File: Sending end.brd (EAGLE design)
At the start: 100 x 80 mm, 17 parts, among them IC1 MEGA8-P

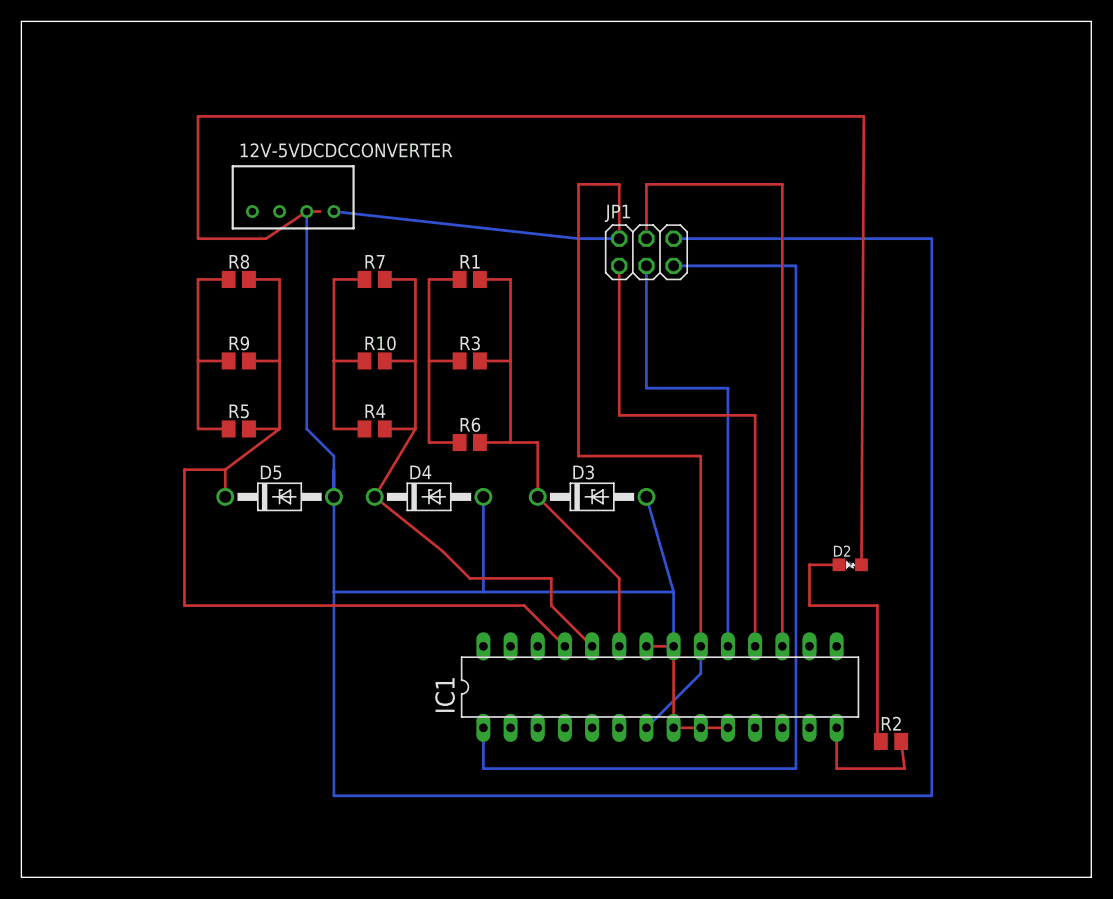
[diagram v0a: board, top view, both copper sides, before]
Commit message: The Sending End layout before going through the checklist
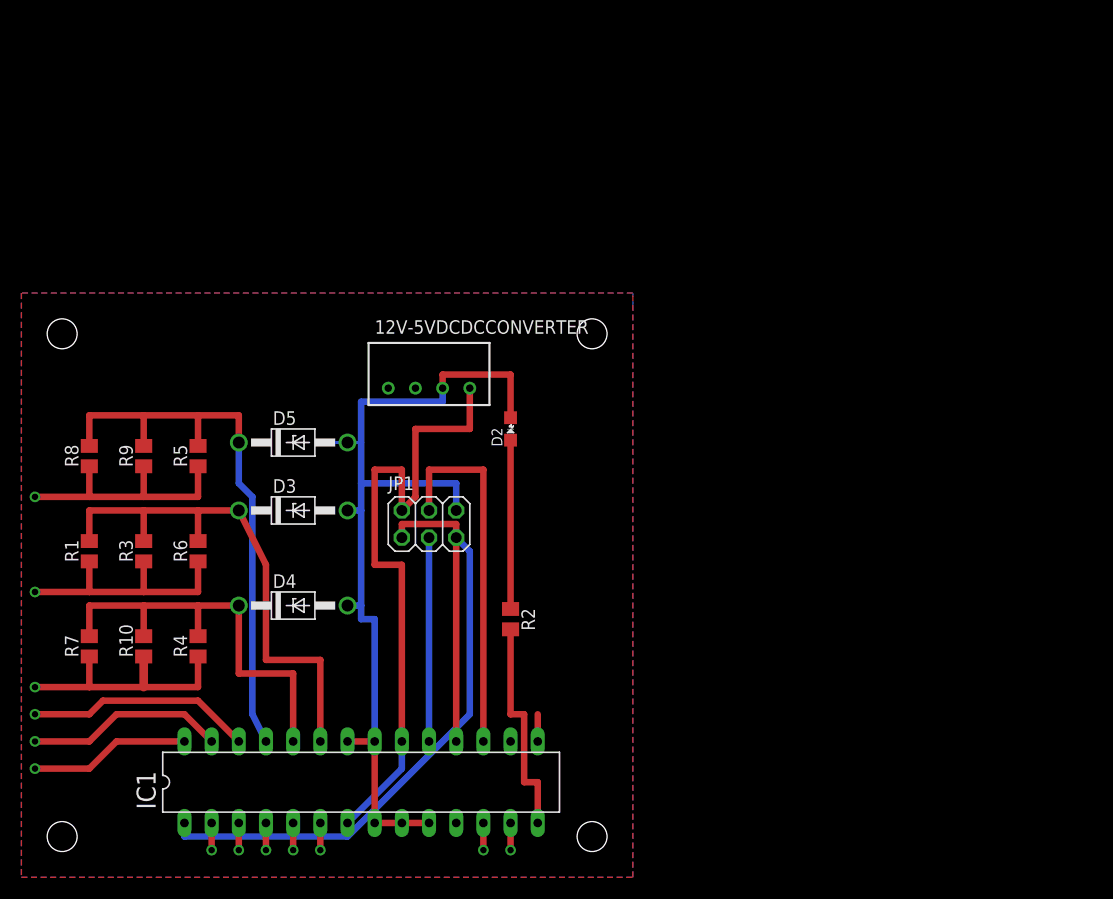
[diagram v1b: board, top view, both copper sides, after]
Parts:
- moved R1 43.7 mm to (6.35, 30.5), turned to 90 degrees
- moved R7 43.4 mm to (6.35, 21.6), turned to 90 degrees
- moved R2 37.4 mm to (45.7, 24.1), turned to 270 degrees
- moved R3 35.3 mm to (11.4, 30.5), turned to 90 degrees
- moved R10 34.3 mm to (11.4, 21.6), turned to 90 degrees
- moved D2 34.2 mm to (45.7, 41.9), turned to 90 degrees
- moved JP1 32.5 mm to (38.1, 33.0)
- moved IC1 29.3 mm to (31.8, 8.89)
- moved D3 28.0 mm to (25.4, 34.3)
- moved R6 27.4 mm to (16.5, 30.5), turned to 90 degrees
- moved R4 26.2 mm to (16.5, 21.6), turned to 90 degrees
- moved R8 21.6 mm to (6.35, 39.4), turned to 90 degrees
- moved 12V-5VDCDCCONVERTER 20.8 mm to (38.1, 45.7)
- moved D4 16.3 mm to (25.4, 25.4)
- moved R9 12.6 mm to (11.4, 39.4), turned to 90 degrees
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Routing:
- net GND: track 388.3 -> 86.6 mm
- net N$7: track 91.4 -> 49.7 mm
- net VCC: track 100.0 -> 61.1 mm
- net N$3: track 85.1 -> 53.9 mm
- net N$23: track 61.0 -> 34.3 mm
- net N$25: track 43.2 -> 19.1 mm
- net N$24: track 48.3 -> 26.7 mm
- net N$11: track 0.00 -> 21.2 mm, vias 0 -> 1
- net N$12: track 0.00 -> 18.6 mm, vias 0 -> 1
- net N$2: track 57.2 -> 40.3 mm
- net N$13: track 0.00 -> 15.0 mm, vias 0 -> 1
- net N$6: track 25.9 -> 15.8 mm
- net N$20: track 12.7 -> 20.6 mm
- net N$21: track 0.00 -> 2.54 mm
- net N$19: track 0.00 -> 2.54 mm, vias 0 -> 1
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- added copper zone on layer 16, net N$4
- added copper zone on layer 1, net N$9
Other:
- board outline removed
- board text added: "Night Rider: Transmission Board"
- board text added: "Solomon Cooper Jessie Bates Brandon Valentine Abdullah Al Madan"

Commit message: Sending End Layout before meeting with Greenberg
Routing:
- net N$7: track 49.7 -> 62.0 mm
- net N$21: track 2.54 -> 13.0 mm, vias 0 -> 1
- net N$24: track 26.7 -> 21.2 mm
- net VCC: track 61.1 -> 58.3 mm
- net GND: track 86.6 -> 84.3 mm
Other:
- board text added: "Version 2.0"
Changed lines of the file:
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@@
 <setting verticaltext="up"/>
 </settings>
-<grid distance="0.05" unitdist="inch" unit="inch" style="lines" multiple="1" display="no" altdistance="0.025" altunitdist="inch" altunit="inch"/>
+<grid distance="0.01" unitdist="inch" unit="inch" style="lines" multiple="1" display="yes" altdistance="0.025" altunitdist="inch" altunit="inch"/>
 <layers>
 <layer number="1" name="Top" color="4" fill="1" visible="yes" active="yes"/>
@@
 <hole x="53.34" y="3.81" drill="2.8"/>
 <hole x="53.34" y="50.8" drill="2.8"/>
-<text x="6.35" y="50.8" size="1.27" layer="48" distance="47">Night Rider: Transmission Board</text>
-<text x="6.35" y="44.45" size="1.016" layer="48">Solomon Cooper
+<text x="6.604" y="52.578" size="1.27" layer="21" distance="47">Night Rider: Transmission Board</text>
+<text x="6.096" y="44.958" size="1.27" layer="21">Solomon Cooper
 Jessie Bates
 Brandon Valentine
 Abdullah Al Madan</text>
+<text x="5.08" y="1.27" size="1.4224" layer="21">Version 2.0</text>
 </plain>
 <attributes>
@@
 <wire x1="33.02" y1="12.7" x2="33.02" y2="5.08" width="0.6096" layer="1"/>
 <wire x1="31.75" y1="36.83" x2="31.75" y2="40.64" width="0.6096" layer="16"/>
-<wire x1="27.94" y1="40.64" x2="30.48" y2="40.64" width="0.254" layer="16"/>
+<wire x1="30.226" y1="40.64" x2="30.48" y2="40.64" width="0.254" layer="16"/>
 <wire x1="30.48" y1="40.64" x2="31.75" y2="40.64" width="0.254" layer="16"/>
 <wire x1="31.75" y1="34.29" x2="31.75" y2="36.83" width="0.6096" layer="16"/>
@@
 <wire x1="7.62" y1="16.51" x2="6.35" y2="15.24" width="0.6096" layer="1"/>
 <wire x1="6.35" y1="15.24" x2="1.27" y2="15.24" width="0.6096" layer="1"/>
-<via x="1.27" y="15.24" extent="1-16" drill="0.6" shape="square"/>
+<via x="1.27" y="15.24" extent="1-16" drill="0.5"/>
 </signal>
 <signal name="N$12">
@@
 <wire x1="8.89" y1="15.24" x2="6.35" y2="12.7" width="0.6096" layer="1"/>
 <wire x1="6.35" y1="12.7" x2="1.27" y2="12.7" width="0.6096" layer="1"/>
-<via x="1.27" y="12.7" extent="1-16" drill="0.6" shape="square"/>
+<via x="1.27" y="12.7" extent="1-16" drill="0.5"/>
 </signal>
 <signal name="N$13">
@@
 <wire x1="8.89" y1="12.7" x2="6.35" y2="10.16" width="0.6096" layer="1"/>
 <wire x1="6.35" y1="10.16" x2="1.27" y2="10.16" width="0.6096" layer="1"/>
-<via x="1.27" y="10.16" extent="1-16" drill="0.6" shape="square"/>
+<via x="1.27" y="10.16" extent="1-16" drill="0.5"/>
 </signal>
 <signal name="N$14">
 <contactref element="IC1" pad="2"/>
 <wire x1="17.78" y1="5.08" x2="17.78" y2="2.54" width="0.6096" layer="1"/>
-<via x="17.78" y="2.54" extent="1-16" drill="0.6" shape="square"/>
+<via x="17.78" y="2.54" extent="1-16" drill="0.5"/>
 </signal>
 <signal name="N$15">
 <contactref element="IC1" pad="3"/>
 <wire x1="20.32" y1="5.08" x2="20.32" y2="2.54" width="0.6096" layer="1"/>
-<via x="20.32" y="2.54" extent="1-16" drill="0.6" shape="square"/>
+<via x="20.32" y="2.54" extent="1-16" drill="0.5"/>
 </signal>
 <signal name="N$16">
 <contactref element="IC1" pad="4"/>
 <wire x1="22.86" y1="5.08" x2="22.86" y2="2.54" width="0.6096" layer="1"/>
-<via x="22.86" y="2.54" extent="1-16" drill="0.6" shape="square"/>
+<via x="22.86" y="2.54" extent="1-16" drill="0.5"/>
 </signal>
 <signal name="N$17">
 <contactref element="IC1" pad="6"/>
 <wire x1="27.94" y1="5.08" x2="27.94" y2="2.54" width="0.6096" layer="1"/>
-<via x="27.94" y="2.54" extent="1-16" drill="0.6" shape="square"/>
+<via x="27.94" y="2.54" extent="1-16" drill="0.5"/>
 </signal>
 <signal name="N$18">
 <contactref element="IC1" pad="12"/>
 <wire x1="43.18" y1="5.08" x2="43.18" y2="2.54" width="0.6096" layer="1"/>
-<via x="43.18" y="2.54" extent="1-16" drill="0.6" shape="square"/>
+<via x="43.18" y="2.54" extent="1-16" drill="0.5"/>
 </signal>
 <signal name="N$19">
 <contactref element="IC1" pad="13"/>
 <wire x1="45.72" y1="5.08" x2="45.72" y2="2.54" width="0.6096" layer="1"/>
-<via x="45.72" y="2.54" extent="1-16" drill="0.6" shape="square"/>
+<via x="45.72" y="2.54" extent="1-16" drill="0.5"/>
 </signal>
 <signal name="N$20">
@@
 <signal name="N$21">
 <contactref element="IC1" pad="15"/>
-<wire x1="48.26" y1="12.7" x2="48.26" y2="15.24" width="0.6096" layer="1"/>
+<wire x1="48.26" y1="12.7" x2="51.054" y2="12.7" width="0.6096" layer="1"/>
+<wire x1="51.054" y1="12.7" x2="51.054" y2="2.54" width="0.6096" layer="1"/>
+<via x="51.054" y="2.54" extent="1-16" drill="0.5"/>
 </signal>
 <signal name="N$22">
@@
 <contactref element="IC1" pad="18"/>
 <contactref element="JP1" pad="1"/>
-<wire x1="35.56" y1="31.75" x2="35.56" y2="33.02" width="0.6096" layer="1"/>
-<wire x1="35.56" y1="33.02" x2="40.64" y2="33.02" width="0.6096" layer="1"/>
-<wire x1="40.64" y1="33.02" x2="40.64" y2="12.7" width="0.6096" layer="1"/>
+<wire x1="35.56" y1="31.75" x2="35.56" y2="30.226" width="0.6096" layer="1"/>
+<wire x1="35.56" y1="30.226" x2="40.64" y2="25.4" width="0.6096" layer="1"/>
+<wire x1="40.64" y1="25.4" x2="40.64" y2="12.7" width="0.6096" layer="1"/>
 </signal>
 <signal name="N$25">
@@
 <contactref element="IC1" pad="1"/>
 <contactref element="JP1" pad="5"/>
-<wire x1="15.24" y1="3.81" x2="15.24" y2="5.08" width="0.6096" layer="16"/>
-<wire x1="30.48" y1="3.81" x2="15.24" y2="3.81" width="0.6096" layer="16"/>
+<wire x1="15.24" y1="1.016" x2="15.24" y2="5.08" width="0.6096" layer="16"/>
+<wire x1="30.988" y1="1.016" x2="15.24" y2="1.016" width="0.6096" layer="16"/>
 <wire x1="40.64" y1="31.75" x2="41.91" y2="30.48" width="0.6096" layer="16"/>
 <wire x1="41.91" y1="30.48" x2="41.91" y2="15.24" width="0.6096" layer="16"/>
-<wire x1="41.91" y1="15.24" x2="30.48" y2="3.81" width="0.6096" layer="16"/>
+<wire x1="41.91" y1="15.24" x2="41.91" y2="1.016" width="0.6096" layer="16"/>
+<wire x1="41.91" y1="1.016" x2="30.988" y2="1.016" width="0.6096" layer="16"/>
 </signal>
 <signal name="VCC">
@@
 <wire x1="35.56" y1="10.16" x2="30.48" y2="5.08" width="0.6096" layer="16"/>
 <wire x1="35.56" y1="12.7" x2="35.56" y2="10.16" width="0.6096" layer="16"/>
-<wire x1="35.56" y1="34.29" x2="36.83" y2="35.56" width="0.6096" layer="1"/>
-<wire x1="36.83" y1="35.56" x2="36.83" y2="41.91" width="0.6096" layer="1"/>
-<wire x1="36.83" y1="41.91" x2="41.91" y2="41.91" width="0.6096" layer="1"/>
+<wire x1="35.56" y1="34.29" x2="35.56" y2="38.354" width="0.6096" layer="1"/>
+<wire x1="35.56" y1="38.354" x2="38.608" y2="41.91" width="0.6096" layer="1"/>
+<wire x1="38.608" y1="41.91" x2="41.91" y2="41.91" width="0.6096" layer="1"/>
 <wire x1="41.91" y1="41.91" x2="41.91" y2="45.72" width="0.6096" layer="1"/>
-<wire x1="35.56" y1="29.21" x2="35.56" y2="12.7" width="0.6096" layer="1"/>
-<wire x1="33.02" y1="29.21" x2="35.56" y2="29.21" width="0.6096" layer="1"/>
+<wire x1="35.56" y1="26.416" x2="35.56" y2="12.7" width="0.6096" layer="1"/>
+<wire x1="33.02" y1="29.21" x2="35.56" y2="26.416" width="0.6096" layer="1"/>
 <wire x1="35.56" y1="34.29" x2="35.56" y2="38.1" width="0.6096" layer="1"/>
 <wire x1="35.56" y1="38.1" x2="33.02" y2="38.1" width="0.6096" layer="1"/>
@@
 <contactref element="IC1" pad="5"/>
 <wire x1="25.4" y1="5.08" x2="25.4" y2="2.54" width="0.6096" layer="1"/>
-<via x="25.4" y="2.54" extent="1-16" drill="0.6" shape="square"/>
+<via x="25.4" y="2.54" extent="1-16" drill="0.5"/>
 </signal>
 <signal name="N$2">
@@
 <wire x1="11.43" y1="26.67" x2="11.43" y2="29.53" width="0.6096" layer="1"/>
 <wire x1="6.35" y1="26.67" x2="1.27" y2="26.67" width="0.6096" layer="1"/>
-<via x="1.27" y="26.67" extent="1-16" drill="0.6" shape="square"/>
+<via x="1.27" y="26.67" extent="1-16" drill="0.5"/>
 </signal>
 <signal name="N$8">
@@
 <wire x1="11.43" y1="17.78" x2="11.43" y2="20.64" width="0.8128" layer="1"/>
 <wire x1="6.35" y1="17.78" x2="1.27" y2="17.78" width="0.6096" layer="1"/>
-<via x="1.27" y="17.78" extent="1-16" drill="0.6" shape="square"/>
+<via x="1.27" y="17.78" extent="1-16" drill="0.5"/>
 </signal>
 <signal name="N$10">
@@
 <wire x1="11.43" y1="35.56" x2="11.43" y2="38.42" width="0.6096" layer="1"/>
 <wire x1="6.35" y1="35.56" x2="1.27" y2="35.56" width="0.6096" layer="1"/>
-<via x="1.27" y="35.56" extent="1-16" drill="0.6" shape="square"/>
+<via x="1.27" y="35.56" extent="1-16" drill="0.5"/>
 </signal>
 <signal name="N$4">

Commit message: sending end echematic version 3.0. need more work on the DCDC converter
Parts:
- removed D3, D4, D5: ZPY, diode:DO41Z10
- removed R1, R10, R3, R4, R5, R6, R7, R8, R9: tbd, resistor:M0805
- added C1, C2, C3, C4, C5, C6, C7: (no value), rcl:C0805
- added R12, R13, R14, R15, R16, R17, R18, R19, R20: tbd, resistor:M0805
- added R21: 10k, resistor:M0805
- added T1, T2, T3: (no value), zetex:SOT-23
- added TP1, TP10, TP11, TP12, TP13, TP14, TP2, TP3, TP4, TP5, TP6, TP7, TP8, TP9: PTR1PAD1-20, testpad:P1-20
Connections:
- removed net N$10: R5.1, R8.1, R9.1
- removed net N$2: D4.C, IC1.24, R10.2, R4.2, R7.2
- removed net N$26: D3.C, IC1.23, R1.2, R3.2, R6.2
- removed net N$3: D5.C, IC1.25, R5.2, R8.2, R9.2
- removed net N$5: R1.1, R3.1, R6.1
- removed net N$8: R10.1, R4.1, R7.1
- new net AVCC: IC1.20
- new net LEFT: R17.1
- new net N$12: IC1.9, TP1.TP
- new net N$31: C1.2, C6.2
- new net N$34: C4.1, R16.2, R17.2, T2.3
- new net N$35: R15.2, T2.1
- new net N$37: C5.1, R19.2, R20.2, T3.3
- new net N$39: IC1.10, TP3.TP
- new net N$40: IC1.11, TP8.TP
- new net N$41: IC1.26, R12.2, T1.1
- new net RIGHT: R14.1
- new net STOP: R20.1
- new net VCC1: C7.1
- net GND: now also C2.2, C3.2, C4.2, C5.2, C7.2, R13.1, R16.1, R19.1, T1.2, T2.2, T3.2; no longer D3.A, D4.A, D5.A, IC1.10, IC1.9
- net N$1: now also TP5.TP
- net N$11: now also C3.1, R13.2, R14.2, T1.3; no longer IC1.26
- net N$13: now also R18.2, T3.1
- net N$15: now also TP4.TP
- net N$16: now also TP7.TP
- net N$17: now also TP6.TP
- net N$18: now also TP9.TP
- net N$19: now also TP10.TP
- net N$21: now also TP13.TP
- net N$22: now also TP14.TP
- net N$27: now also TP11.TP
- net N$28: now also TP12.TP
- net N$7: now also R21.2
- net VCC: now also C1.1, C6.1, R12.1, R15.1, R18.1, R21.1; no longer IC1.20
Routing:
- net N$3: track 53.9 -> 0.00 mm
- net N$26: track 49.8 -> 0.00 mm
- net N$2: track 40.3 -> 0.00 mm
- net N$8: track 23.8 -> 0.00 mm, vias 1 -> 0
- net N$5: track 23.8 -> 0.00 mm, vias 1 -> 0
- net N$10: track 23.8 -> 0.00 mm, vias 1 -> 0
- net N$41: track 0.00 -> 21.2 mm, vias 0 -> 1
- net N$11: track 21.2 -> 0.00 mm, vias 1 -> 0
- net VCC: track 58.3 -> 42.1 mm
- net GND: track 84.3 -> 75.2 mm
- net N$7: track 62.0 -> 57.9 mm
- net N$15: track 2.54 -> 0.00 mm, vias 1 -> 0

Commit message: the sending end schematic Version 4.0 it has the following modifications: DCtoDCconverter connected as desired; the diode for transmission has an NMOS transistor to amplify the current
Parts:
- removed 12V-5VDCDCCONVERTER: TME1205S, traco-electronic:TME
- removed D2: HSMXC670, opto-transmittter-hp:HSMXC670
- added D1: HSMXC670, opto-transmittter-hp:HSMXC670
- added JP2: (no value), pinhead:1X02
- added L1, R1, R3: tbd, resistor:M0805
- added T4: (no value), zetex:SOT-23
- added TP15: PTR1PAD1-20, testpad:P1-20
- added U$1: (no value), nka1205sc:NKA1205SC
- moved TP11 88.9 mm to (1.78, -234.4)
- moved TP12 88.9 mm to (1.78, -239.8)
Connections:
- removed net AVCC: IC1.20
- removed net N$14: IC1.2
- removed net N$31: C1.2, C6.2
- removed net N$42: IC1.27
- removed net VCC1: C7.1
- new net N$2: R1.2, R2.1, T4.3
- new net N$26: JP2.2, U$1.-VIN
- new net N$29: IC1.25, TP15.TP
- new net N$3: R3.1, T4.1
- new net N$30: JP2.1, U$1.+VIN
- new net N$5: IC1.2, TP2.TP
- new net N$8: L1.2, U$1.+VOUT
- net GND: now also C1.2, C6.2, D1.K, R1.1, U$1.-VOUT; no longer 12V-5VDCDCCONVERTER.3, D2.K
- net N$27: now also IC1.23; no longer 12V-5VDCDCCONVERTER.2
- net N$28: now also IC1.24; no longer 12V-5VDCDCCONVERTER.1
- net N$35: now also IC1.27
- net N$6: now also D1.A, T4.2; no longer D2.A, R2.1
- net VCC: now also C2.1, C7.1, IC1.20, L1.1, R3.2; no longer 12V-5VDCDCCONVERTER.4
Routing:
- net N$42: track 18.6 -> 0.00 mm, vias 1 -> 0
- net N$35: track 0.00 -> 18.6 mm, vias 0 -> 1
- net N$6: track 15.8 -> 0.00 mm
- net GND: track 75.2 -> 62.2 mm
- net VCC: track 42.1 -> 38.2 mm
- net N$14: track 2.54 -> 0.00 mm, vias 1 -> 0
